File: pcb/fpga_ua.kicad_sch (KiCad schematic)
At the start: 17 parts, among them U1101 XC7A100T-FTG256, Y1101 ECS-2520MV-080-BN-TR

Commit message: start layout
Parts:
- removed U1101: XC7A100T-FTG256, fpga:BGA256C100P16X16_1700X1700X155, symbol FPGA_Xilinx_Artix7:XC7A100T-FTG256
- added U666: XC7A75T-FTG256, Package_BGA:Xilinx_FTG256, symbol FPGA_Xilinx_Artix7:XC7A75T-FTG256
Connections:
- net +3V3: now also U666.A16 (VCCO_15), U666.B13 (VCCO_15), U666.C10 (VCCO_15), U666.E14 (VCCO_15), U666.H15 (VCCO_15), U666.J12 (VCCO_15), U666.L16 (VCCO_14), U666.M13 (VCCO_14), U666.N10 (VCCO_14), U666.P7 (VCCO_14), U666.R14 (VCCO_14), U666.T11 (VCCO_14)
- net FGPA_MCU_EXTRA2: now also U666.N12 (IO_L13N_T2_MRCC_14)
- net FPGA_DEBUG_LED_BLOCK14_1: now also U666.R5 (IO_L23P_T3_A03_D19_14)
- net FPGA_DEBUG_LED_BLOCK15_1: now also U666.C11 (IO_L11P_T1_SRCC_15)
- net FPGA_OSCILLATOR_CLOCK: now also U666.N11 (IO_L13P_T2_MRCC_14)
- net SRAM_#CE: now also U666.P8 (IO_L20P_T3_A08_D24_14)
- net SRAM_#LB: now also U666.R8 (IO_L20N_T3_A07_D23_14)
- net SRAM_#OE: now also U666.T7 (IO_L21P_T3_DQS_14)
- net SRAM_#UB: now also U666.T8 (IO_L21N_T3_DQS_A06_D22_14)
- net SRAM_#WE: now also U666.T9 (IO_L22P_T3_A05_D21_14)
- net SRAM_A0: now also U666.J13 (IO_L1P_T0_D00_MOSI_14)
- net SRAM_A1: now also U666.J14 (IO_L1N_T0_D01_DIN_14)
- net SRAM_A10: now also U666.L12 (IO_L6P_T0_FCS_B_14)
- net SRAM_A11: now also U666.M12 (IO_L6N_T0_D08_VREF_14)
- net SRAM_A12: now also U666.M16 (IO_L7P_T1_D09_14)
- net SRAM_A13: now also U666.N16 (IO_L7N_T1_D10_14)
- net SRAM_A14: now also U666.P15 (IO_L8P_T1_D11_14)
- net SRAM_A15: now also U666.P16 (IO_L8N_T1_D12_14)
- net SRAM_A16: now also U666.R15 (IO_L9P_T1_DQS_14)
- net SRAM_A17: now also U666.R16 (IO_L9N_T1_DQS_D13_14)
- net SRAM_A18: now also U666.T14 (IO_L10P_T1_D14_14)
- net SRAM_A19: now also U666.T15 (IO_L10N_T1_D15_14)
- net SRAM_A2: now also U666.K15 (IO_L2P_T0_D02_14)
- net SRAM_A3: now also U666.K16 (IO_L2N_T0_D03_14)
- net SRAM_A4: now also U666.L15 (IO_L3P_T0_DQS_PUDC_B_14)
- net SRAM_A5: now also U666.M15 (IO_L3N_T0_DQS_EMCCLK_14)
- net SRAM_A6: now also U666.L14 (IO_L4P_T0_D04_14)
- net SRAM_A7: now also U666.M14 (IO_L4N_T0_D05_14)
- net SRAM_A8: now also U666.K13 (IO_L5P_T0_D06_14)
- net SRAM_A9: now also U666.L13 (IO_L5N_T0_D07_14)
- net SRAM_D0: now also U666.N13 (IO_L11P_T1_SRCC_14)
- net SRAM_D1: now also U666.P13 (IO_L11N_T1_SRCC_14)
- net SRAM_D10: now also U666.R10 (IO_L17P_T2_A14_D30_14)
- net SRAM_D11: now also U666.R11 (IO_L17N_T2_A13_D29_14)
- net SRAM_D12: now also U666.N9 (IO_L18P_T2_A12_D28_14)
- net SRAM_D13: now also U666.P9 (IO_L18N_T2_A11_D27_14)
- net SRAM_D14: now also U666.M6 (IO_L19P_T3_A10_D26_14)
- net SRAM_D15: now also U666.N6 (IO_L19N_T3_A09_D25_VREF_14)
- net SRAM_D2: now also U666.N14 (IO_L12P_T1_MRCC_14)
- net SRAM_D3: now also U666.P14 (IO_L12N_T1_MRCC_14)
- net SRAM_D4: now also U666.P10 (IO_L14P_T2_SRCC_14)
- net SRAM_D5: now also U666.P11 (IO_L14N_T2_SRCC_14)
- net SRAM_D6: now also U666.R12 (IO_L15P_T2_DQS_RDWR_B_14)
- net SRAM_D7: now also U666.T12 (IO_L15N_T2_DQS_DOUT_CSO_B_14)
- net SRAM_D8: now also U666.R13 (IO_L16P_T2_CSI_B_14)
- net SRAM_D9: now also U666.T13 (IO_L16N_T2_A15_D31_14)
- net vga_b1: now also U666.C8 (IO_L1P_T0_AD0P_15)
- net vga_b2: now also U666.C9 (IO_L1N_T0_AD0N_15)
- net vga_b3: now also U666.A8 (IO_L2P_T0_AD8P_15)
- net vga_b4: now also U666.A9 (IO_L2N_T0_AD8N_15)
- net vga_b5: now also U666.B9 (IO_L3P_T0_DQS_AD1P_15)
- net vga_g1: now also U666.A10 (IO_L3N_T0_DQS_AD1N_15)
- net vga_g2: now also U666.B10 (IO_L4P_T0_15)
- net vga_g3: now also U666.B11 (IO_L4N_T0_15)
- net vga_g4: now also U666.B12 (IO_L5P_T0_AD9P_15)
- net vga_g5: now also U666.A12 (IO_L5N_T0_AD9N_15)
- net vga_g6: now also U666.D8 (IO_L6P_T0_15)
- net vga_hsync: now also U666.A15 (IO_L9N_T1_DQS_AD3N_15)
- net vga_r1: now also U666.D9 (IO_L6N_T0_VREF_15)
- net vga_r2: now also U666.A13 (IO_L7P_T1_AD2P_15)
- net vga_r3: now also U666.A14 (IO_L7N_T1_AD2N_15)
- net vga_r4: now also U666.C14 (IO_L8P_T1_AD10P_15)
- net vga_r5: now also U666.B14 (IO_L8N_T1_AD10N_15)
- net vga_vsync: now also U666.C16 (IO_L10P_T1_AD11P_15)

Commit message: change footprint of debug_connector
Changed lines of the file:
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@@
       (effects (font (size 1.27 1.27)) hide)
     )
-    (property "Value" "+3V3" (id 1) (at 267.97 20.32 0))
+    (property "Value" "" (id 1) (at 267.97 20.32 0))
     (property "Footprint" "" (id 2) (at 267.97 24.13 0)
       (effects (font (size 1.27 1.27)) hide)
@@
       (effects (font (size 1.27 1.27)) hide)
     )
-    (property "Value" "+3V3" (id 1) (at 267.97 49.53 0))
+    (property "Value" "" (id 1) (at 267.97 49.53 0))
     (property "Footprint" "" (id 2) (at 267.97 53.34 0)
       (effects (font (size 1.27 1.27)) hide)

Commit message: switch some pins for more erqonomiq layout
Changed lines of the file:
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@@
       (effects (font (size 1.27 1.27)) hide)
     )
-    (property "Value" "" (id 1) (at 267.97 20.32 0))
+    (property "Value" "+3V3" (id 1) (at 267.97 20.32 0))
     (property "Footprint" "" (id 2) (at 267.97 24.13 0)
       (effects (font (size 1.27 1.27)) hide)
@@
       (effects (font (size 1.27 1.27)) hide)
     )
-    (property "Value" "" (id 1) (at 267.97 49.53 0))
+    (property "Value" "+3V3" (id 1) (at 267.97 49.53 0))
     (property "Footprint" "" (id 2) (at 267.97 53.34 0)
       (effects (font (size 1.27 1.27)) hide)

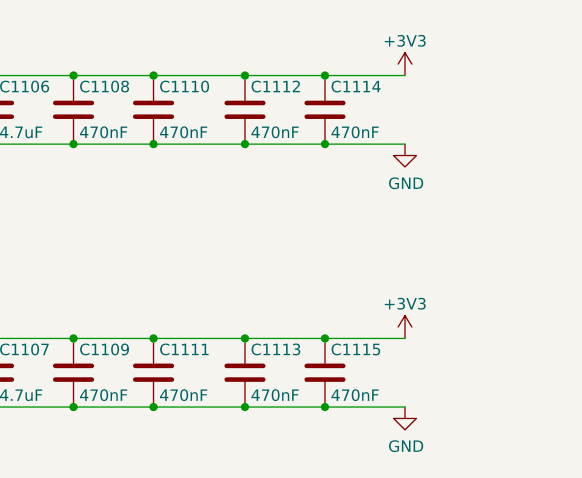
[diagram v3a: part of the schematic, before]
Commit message: psu wiring and power cables
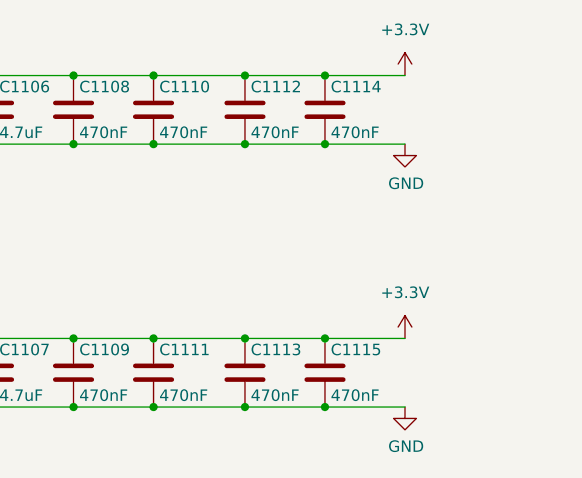
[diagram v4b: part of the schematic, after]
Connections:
- net +3V3 is gone; now on net +3.3V: C1102.1, C1103.1, C1104.1, C1105.1, C1106.1, C1107.1, C1108.1, C1109.1, C1110.1, C1111.1, C1112.1, C1113.1, C1114.1, C1115.1, U666.A16 (VCCO_15), U666.B13 (VCCO_15), U666.C10 (VCCO_15), U666.E14 (VCCO_15), U666.H15 (VCCO_15), U666.J12 (VCCO_15), U666.L16 (VCCO_14), U666.M13 (VCCO_14), U666.N10 (VCCO_14), U666.P7 (VCCO_14), U666.R14 (VCCO_14), U666.T11 (VCCO_14)
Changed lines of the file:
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@@
     (pin "2")
+  )
+  (symbol (lib_id "power:+3.3V") (at 267.97 24.13 0) (unit 1)
+    (in_bom yes) (on_board yes) (fields_autoplaced)
+    (property "Reference" "#PWR?" (id 0) (at 267.97 27.94 0)
+      (effects (font (size 1.27 1.27)) hide)
+    )
+    (property "Value" "+3.3V" (id 1) (at 267.97 19.05 0))
+    (property "Footprint" "" (id 2) (at 267.97 24.13 0)
+      (effects (font (size 1.27 1.27)) hide)
+    )
+    (property "Datasheet" "" (id 3) (at 267.97 24.13 0)
+      (effects (font (size 1.27 1.27)) hide)
+    )
+    (pin "1")
   )
   (symbol (lib_id "Device:C") (at 240.03 57.15 0) (unit 1)
@@
     (pin "1")
     (pin "2")
-  )
-  (symbol (lib_id "power:+3V3") (at 267.97 24.13 0) (unit 1)
-    (in_bom yes) (on_board yes)
-    (property "Reference" "#PWR01103" (id 0) (at 267.97 27.94 0)
-      (effects (font (size 1.27 1.27)) hide)
-    )
-    (property "Value" "+3V3" (id 1) (at 267.97 20.32 0))
-    (property "Footprint" "" (id 2) (at 267.97 24.13 0)
-      (effects (font (size 1.27 1.27)) hide)
-    )
-    (property "Datasheet" "" (id 3) (at 267.97 24.13 0)
-      (effects (font (size 1.27 1.27)) hide)
-    )
-    (pin "1")
   )
   (symbol (lib_id "FPGA_Xilinx_Artix7:XC7A75T-FTG256") (at 102.87 104.14 0) (unit 1)
@@
     (pin "2")
   )
+  (symbol (lib_id "power:+3.3V") (at 267.97 53.34 0) (unit 1)
+    (in_bom yes) (on_board yes) (fields_autoplaced)
+    (property "Reference" "#PWR?" (id 0) (at 267.97 57.15 0)
+      (effects (font (size 1.27 1.27)) hide)
+    )
+    (property "Value" "+3.3V" (id 1) (at 267.97 48.26 0))
+    (property "Footprint" "" (id 2) (at 267.97 53.34 0)
+      (effects (font (size 1.27 1.27)) hide)
+    )
+    (property "Datasheet" "" (id 3) (at 267.97 53.34 0)
+      (effects (font (size 1.27 1.27)) hide)
+    )
+    (pin "1")
+  )
   (symbol (lib_id "ECS-2520MV-080-BN-TR:ECS-2520MV-080-BN-TR") (at 241.3 121.92 0) (unit 1)
     (in_bom yes) (on_board yes) (fields_autoplaced)
@@
     (pin "4")
   )
-  (symbol (lib_id "power:+3V3") (at 267.97 53.34 0) (unit 1)
-    (in_bom yes) (on_board yes)
-    (property "Reference" "#PWR01105" (id 0) (at 267.97 57.15 0)
-      (effects (font (size 1.27 1.27)) hide)
-    )
-    (property "Value" "+3V3" (id 1) (at 267.97 49.53 0))
-    (property "Footprint" "" (id 2) (at 267.97 53.34 0)
-      (effects (font (size 1.27 1.27)) hide)
-    )
-    (property "Datasheet" "" (id 3) (at 267.97 53.34 0)
-      (effects (font (size 1.27 1.27)) hide)
-    )
-    (pin "1")
-  )
   (symbol (lib_id "Device:C") (at 205.74 57.15 0) (unit 1)

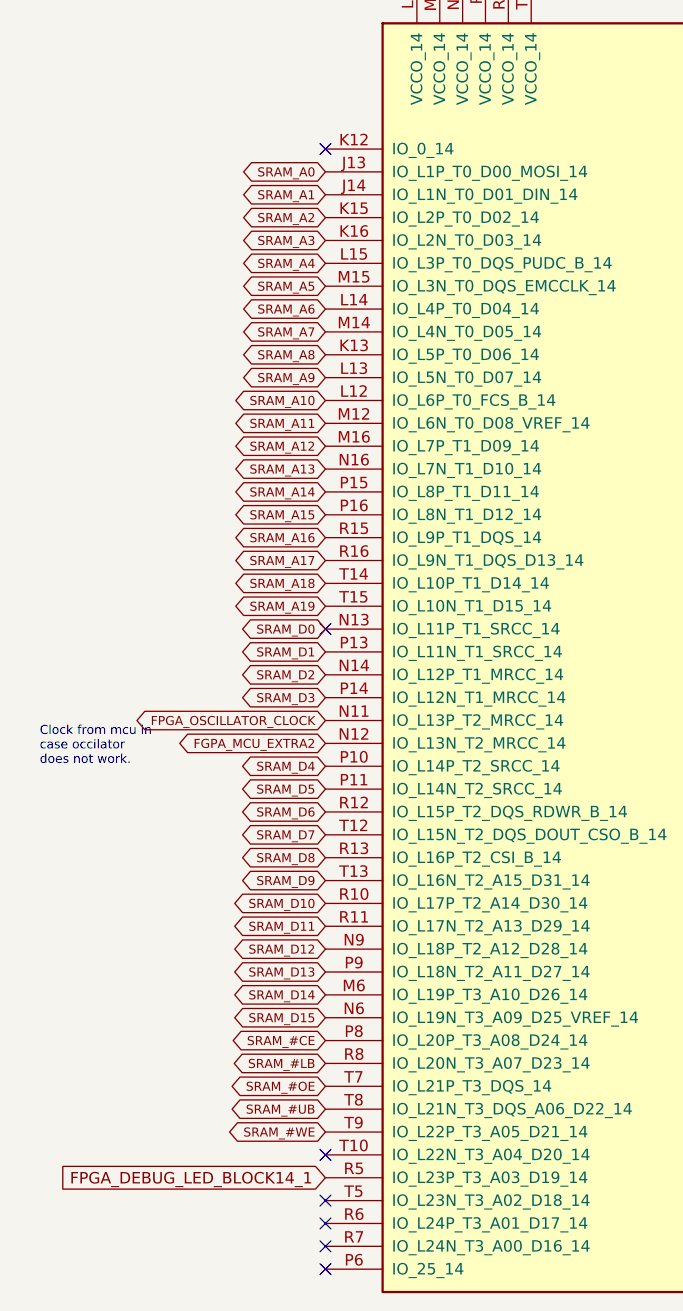
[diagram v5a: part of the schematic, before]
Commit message: change location of stram pin
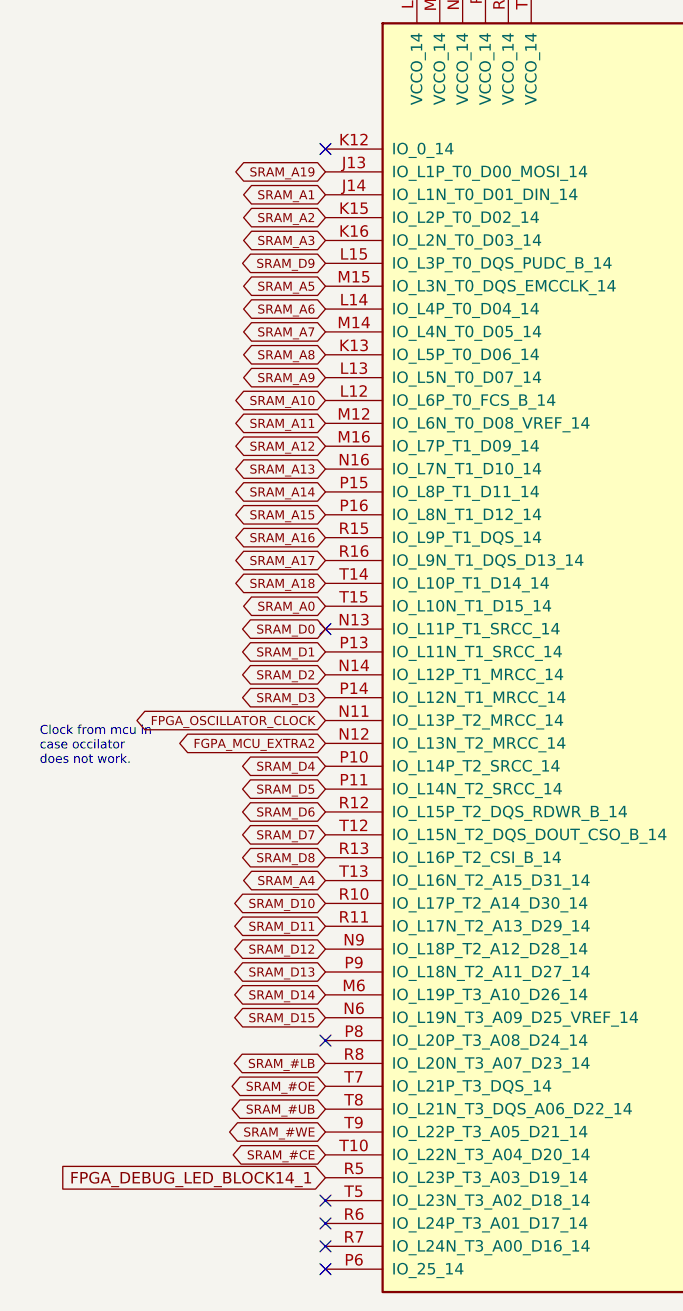
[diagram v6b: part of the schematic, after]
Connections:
- net SRAM_#CE: now also U666.T10 (IO_L22N_T3_A04_D20_14); no longer U666.P8 (IO_L20P_T3_A08_D24_14)
- net SRAM_A0: now also U666.T15 (IO_L10N_T1_D15_14); no longer U666.J13 (IO_L1P_T0_D00_MOSI_14)
- net SRAM_A19: now also U666.J13 (IO_L1P_T0_D00_MOSI_14); no longer U666.T15 (IO_L10N_T1_D15_14)
- net SRAM_A4: now also U666.T13 (IO_L16N_T2_A15_D31_14); no longer U666.L15 (IO_L3P_T0_DQS_PUDC_B_14)
- net SRAM_D9: now also U666.L15 (IO_L3P_T0_DQS_PUDC_B_14); no longer U666.T13 (IO_L16N_T2_A15_D31_14)
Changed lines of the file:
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@@
   (junction (at 261.62 135.89) (diameter 0) (color 0 0 0 0)
   )
+  (no_connect (at 52.07 149.86))
   (no_connect (at 153.67 132.08))
   (no_connect (at 153.67 134.62))
@@
   (no_connect (at 153.67 124.46))
   (no_connect (at 153.67 127))
-  (no_connect (at 52.07 162.56))
   (no_connect (at 52.07 167.64))
   (no_connect (at 52.07 170.18))
@@
     (effects (font (size 1 1)) (justify left bottom))
   )
-  (global_label "SRAM_A4" (shape bidirectional) (at 52.07 63.5 180) (fields_autoplaced)
-    (effects (font (size 1 1)) (justify right))
-    (property "Intersheet References" "${INTERSHEET_REFS}" (id 0) (at 43.6462 63.4375 0)
-      (effects (font (size 1 1)) (justify right) hide)
-    )
-  )
   (global_label "SRAM_D10" (shape bidirectional) (at 52.07 134.62 180) (fields_autoplaced)
     (effects (font (size 1 1)) (justify right))
     (property "Intersheet References" "${INTERSHEET_REFS}" (id 0) (at 42.551 134.5575 0)
-      (effects (font (size 1 1)) (justify right) hide)
-    )
-  )
-  (global_label "SRAM_A0" (shape bidirectional) (at 52.07 53.34 180) (fields_autoplaced)
-    (effects (font (size 1 1)) (justify right))
-    (property "Intersheet References" "${INTERSHEET_REFS}" (id 0) (at 43.6462 53.2775 0)
       (effects (font (size 1 1)) (justify right) hide)
     )
@@
     )
   )
-  (global_label "SRAM_#CE" (shape bidirectional) (at 52.07 149.86 180) (fields_autoplaced)
-    (effects (font (size 1 1)) (justify right))
-    (property "Intersheet References" "${INTERSHEET_REFS}" (id 0) (at 42.551 149.7975 0)
-      (effects (font (size 1 1)) (justify right) hide)
-    )
-  )
   (global_label "SRAM_A15" (shape bidirectional) (at 52.07 91.44 180) (fields_autoplaced)
     (effects (font (size 1 1)) (justify right))
@@
     )
   )
+  (global_label "SRAM_A19" (shape bidirectional) (at 52.07 53.34 180) (fields_autoplaced)
+    (effects (font (size 1 1)) (justify right))
+    (property "Intersheet References" "${INTERSHEET_REFS}" (id 0) (at 42.6938 53.2775 0)
+      (effects (font (size 1 1)) (justify right) hide)
+    )
+  )
   (global_label "SRAM_A8" (shape bidirectional) (at 52.07 73.66 180) (fields_autoplaced)
     (effects (font (size 1 1)) (justify right))
@@
     )
   )
-  (global_label "SRAM_A19" (shape bidirectional) (at 52.07 101.6 180) (fields_autoplaced)
-    (effects (font (size 1 1)) (justify right))
-    (property "Intersheet References" "${INTERSHEET_REFS}" (id 0) (at 42.6938 101.5375 0)
-      (effects (font (size 1 1)) (justify right) hide)
-    )
-  )
   (global_label "SRAM_#LB" (shape bidirectional) (at 52.07 152.4 180) (fields_autoplaced)
     (effects (font (size 1 1)) (justify right))
@@
     )
   )
-  (global_label "SRAM_D9" (shape bidirectional) (at 52.07 132.08 180) (fields_autoplaced)
-    (effects (font (size 1 1)) (justify right))
-    (property "Intersheet References" "${INTERSHEET_REFS}" (id 0) (at 43.5033 132.0175 0)
-      (effects (font (size 1 1)) (justify right) hide)
-    )
-  )
   (global_label "SRAM_D12" (shape bidirectional) (at 52.07 139.7 180) (fields_autoplaced)
     (effects (font (size 1 1)) (justify right))
@@
     )
   )
+  (global_label "SRAM_D9" (shape bidirectional) (at 52.07 63.5 180) (fields_autoplaced)
+    (effects (font (size 1 1)) (justify right))
+    (property "Intersheet References" "${INTERSHEET_REFS}" (id 0) (at 43.5033 63.4375 0)
+      (effects (font (size 1 1)) (justify right) hide)
+    )
+  )
+  (global_label "SRAM_A4" (shape bidirectional) (at 52.07 132.08 180) (fields_autoplaced)
+    (effects (font (size 1 1)) (justify right))
+    (property "Intersheet References" "${INTERSHEET_REFS}" (id 0) (at 43.6462 132.0175 0)
+      (effects (font (size 1 1)) (justify right) hide)
+    )
+  )
+  (global_label "SRAM_#CE" (shape bidirectional) (at 52.07 162.56 180) (fields_autoplaced)
+    (effects (font (size 1 1)) (justify right))
+    (property "Intersheet References" "${INTERSHEET_REFS}" (id 0) (at 42.551 162.4975 0)
+      (effects (font (size 1 1)) (justify right) hide)
+    )
+  )
   (global_label "vga_r5" (shape bidirectional) (at 153.67 91.44 0) (fields_autoplaced)
     (effects (font (size 1 1)) (justify left))
@@
     )
   )
+  (global_label "SRAM_A0" (shape bidirectional) (at 52.07 101.6 180) (fields_autoplaced)
+    (effects (font (size 1 1)) (justify right))
+    (property "Intersheet References" "${INTERSHEET_REFS}" (id 0) (at 43.6462 101.5375 0)
+      (effects (font (size 1 1)) (justify right) hide)
+    )
+  )
